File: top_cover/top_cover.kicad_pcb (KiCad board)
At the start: 2 copper layers, 323.6 x 142.9 mm, 82 parts, among them SW1 SW_Push, SW11 SW_Push, SW12 SW_Push, SW13 SW_Push, SW14 SW_Push, SW15 SW_Push, SW16 SW_Push, SW17 SW_Push, SW18 SW_Push, SW19 SW_Push, SW2 SW_Push, SW20 SW_Push, SW21 SW_Push, SW22 SW_Push, SW23 SW_Push, SW24 SW_Push, SW25 SW_Push, SW26 SW_Push, SW27 SW_Push, SW28 SW_Push, SW29 SW_Push, SW3 SW_Push, SW30 SW_Push, SW31 SW_Push, SW32 SW_Push, SW33 SW_Push, SW34 SW_Push, SW35 SW_Push, SW36 SW_Push, SW37 SW_Push, SW38 SW_Push, SW39 SW_Push, SW4 SW_Push, SW40 SW_Push, SW41 SW_Push, SW42 SW_Push, SW43 SW_Push, SW44 SW_Push, SW45 SW_Push, SW46 SW_Push, SW47 SW_Push, SW48 SW_Push, SW49 SW_Push, SW5 SW_Push, SW50 SW_Push, SW51 SW_Push, SW52 SW_Push, SW53 SW_Push, SW54 SW_Push, SW55 SW_Push, SW56 SW_Push, SW57 SW_Push, SW58 SW_Push, SW59 SW_Push, SW6 SW_Push, SW60 SW_Push, SW61 SW_Push, SW7 SW_Push, SW8 SW_Push, SW9 SW_Push

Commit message: Plates and covers
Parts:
- removed H1, H10, H11, H13, H15, H18, H19, H2, H21, H22, H4, H5, H6, H7: MountingHole, MountingHole:MountingHole_2.2mm_M2
- removed the H17 at (-40.4, 64.3)
- added H12: MountingHole, MountingHole:MountingHole_2.2mm_M2, B.Cu at (146.7, -58.3)
- added H16: MountingHole, MountingHole:MountingHole_2.2mm_M2, B.Cu at (159.4, -9.90)
- added H17: MountingHole, MountingHole:MountingHole_2.2mm_M2, B.Cu at (78.3, 57.5)
- added H17: MountingHole, MountingHole:MountingHole_2.2mm_M2, F.Cu at (-78.3, 57.5)
- added H20: MountingHole, MountingHole:MountingHole_2.2mm_M2, B.Cu at (47.0, -43.6)
- added H3: MountingHole, MountingHole:MountingHole_2.2mm_M2, B.Cu at (129.1, 34.1)
- added H8: MountingHole, MountingHole:MountingHole_2.2mm_M2, B.Cu at (99.7, -54.8)
- added H9: MountingHole, MountingHole:MountingHole_2.2mm_M2, B.Cu at (16.1, 79.6)
- moved H9 96.2 mm to (-16.1, 79.6)
- moved H12 37.6 mm to (-146.7, -58.3)
- moved H16 37.0 mm to (-159.4, -9.90)
- moved H8 26.6 mm to (-99.7, -54.8)
- moved H3 16.1 mm to (-129.1, 34.1)
- moved H20 9.74 mm to (-47.0, -43.6)
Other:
- outline, holes or cut-outs redrawn

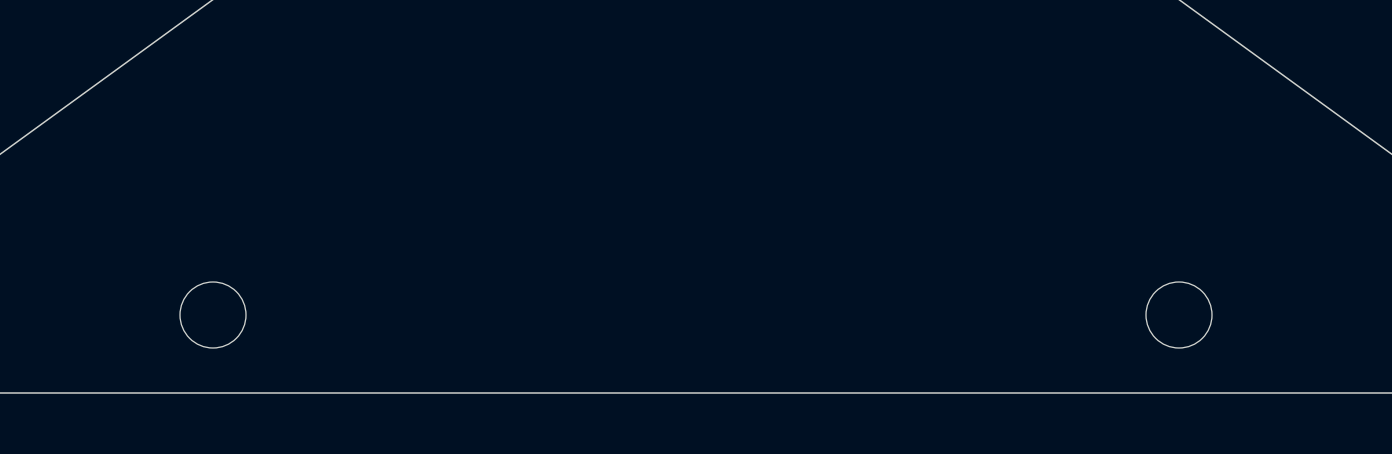
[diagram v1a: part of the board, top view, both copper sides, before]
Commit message: Moving mounting holes
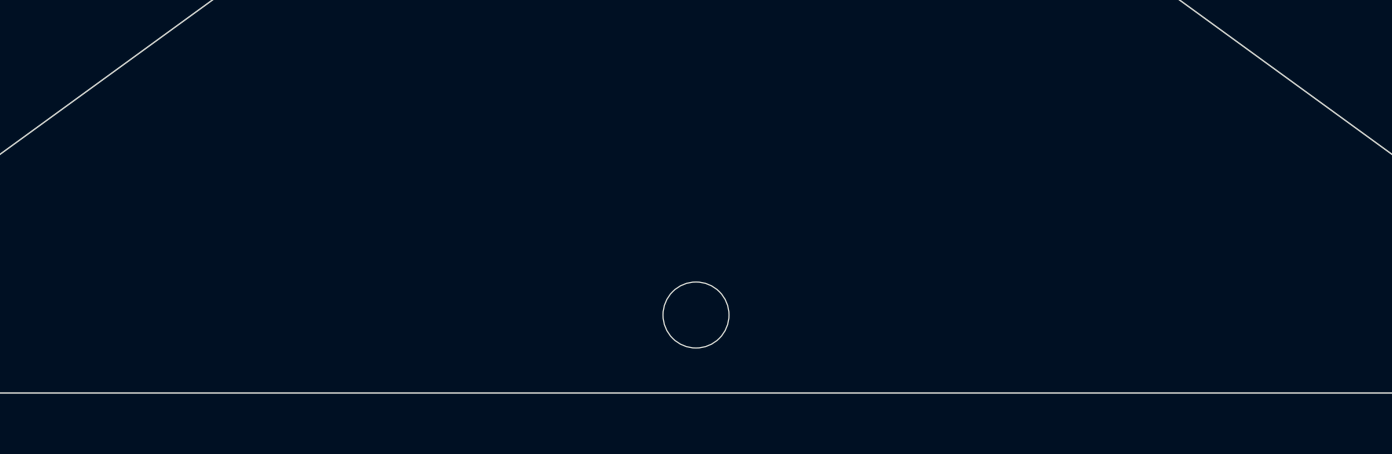
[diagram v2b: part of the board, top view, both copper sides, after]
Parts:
- removed the H9 at (-16.1, 79.6)
- moved H9 16.1 mm to (0.00, 79.6)

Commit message: Working on mounting holes
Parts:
- removed the H17 at (78.3, 57.5)
- added H17: MountingHole, MountingHole:MountingHole_2.2mm_M2, F.Cu at (101.6, 46.5)
- added H17: MountingHole, MountingHole:MountingHole_2.2mm_M2, F.Cu at (56.6, 67.2)
- added H17: MountingHole, MountingHole:MountingHole_2.2mm_M2, F.Cu at (-101.6, 46.5)
- H12, H16, H20, H3, H8, H9: moved to F.Cu
- moved H20 39.6 mm to (11.5, -26.1)
- moved H20 39.6 mm to (-11.5, -26.1)
- moved H8 26.7 mm to (73.2, -51.9)
- moved H8 26.7 mm to (-73.2, -51.9)
- moved H17 23.8 mm to (-56.6, 67.2)
- moved H3 16.6 mm to (-144.1, 27.1)
- moved H3 16.6 mm to (144.1, 27.1)
- moved H16 8.00 mm to (159.2, -17.9)
- moved H16 8.00 mm to (-159.2, -17.9)
- moved H12 0.63 mm to (146.1, -58.1)
- moved H12 0.63 mm to (-146.1, -58.1)

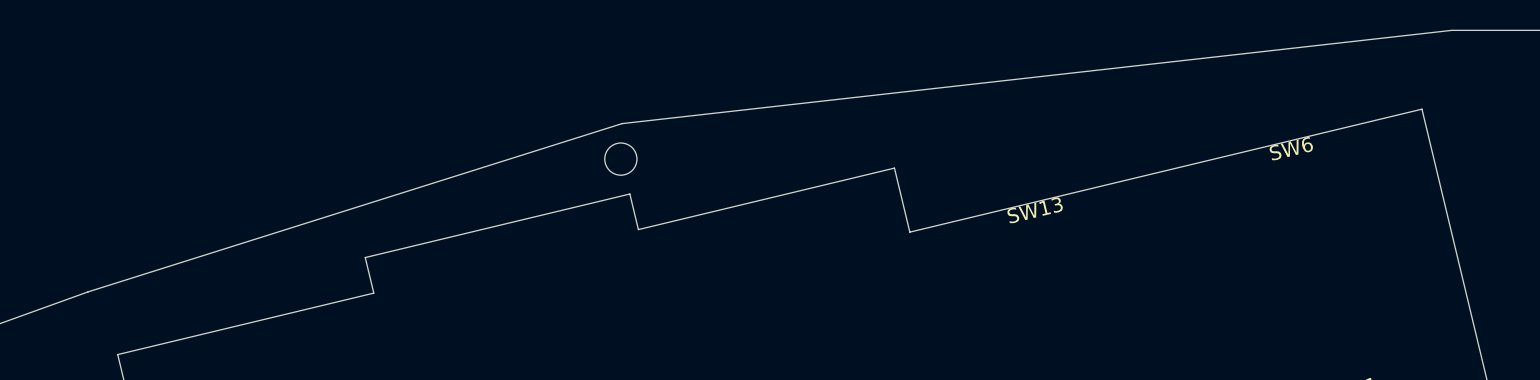
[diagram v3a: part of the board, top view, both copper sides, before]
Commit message: Mountin holes
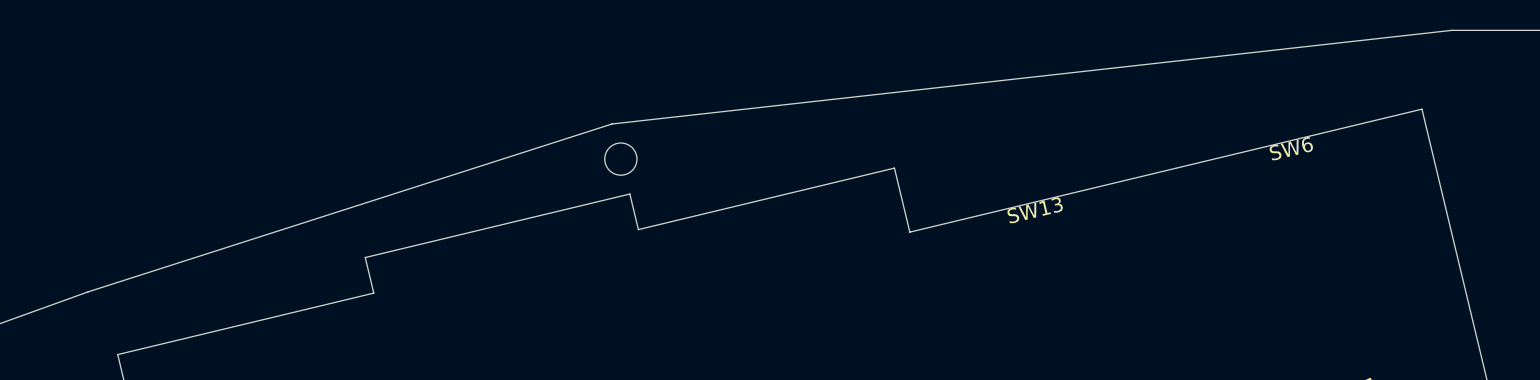
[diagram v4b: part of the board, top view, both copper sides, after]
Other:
- outline, holes or cut-outs redrawn

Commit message: Done with mounting holes, I guess.
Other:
- outline, holes or cut-outs redrawn

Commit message: Making the hole for the encoder optional
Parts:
- ENC2: footprint footprints:Switch_Hole -> footprints:Switch_Optional_Hole
- moved H16 110.9 mm to (109.4, -117.0), turned to 220.5 degrees
- moved H16 110.9 mm to (-132.7, 89.8), turned to 40.5 degrees
- moved H12 108.8 mm to (-148.8, 50.7), turned to 40.5 degrees
- moved H12 108.8 mm to (73.4, -139.1), turned to 220.5 degrees
- moved H3 101.5 mm to (-92.0, 114.2), turned to 40.5 degrees
- moved H3 101.5 mm to (127.2, -73.0), turned to 220.5 degrees
- moved SW53 92.0 mm to (104.3, -82.5), turned to 54 degrees
- moved SW46 92.0 mm to (-97.8, 90.1), turned to 27 degrees
- moved SW37 89.6 mm to (90.6, -92.4), turned to 54 degrees
- moved SW30 89.6 mm to (-105.5, 75.0), turned to 27 degrees
- moved SW6 89.2 mm to (63.0, -112.4), turned to 54 degrees
- moved SW1 89.2 mm to (-120.9, 44.7), turned to 27 degrees
- moved SW21 88.6 mm to (76.8, -102.4), turned to 54 degrees
- moved SW14 88.6 mm to (-113.2, 59.8), turned to 27 degrees
- moved SW61 80.1 mm to (93.7, -67.9), turned to 54 degrees
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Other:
- board size 323.6 x 142.9 mm -> 294.4 x 268.4 mm

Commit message: Working on top cover
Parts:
- removed ENC2: Switch Hole, footprints:Switch_Optional_Hole
- removed the H12 at (73.4, -139.1)
- removed the H12 at (-148.8, 50.7)
- removed the H16 at (109.4, -117.0)
- removed the H16 at (-132.7, 89.8)
- removed H17 (x4), H8 (x2), H9: MountingHole, MountingHole:MountingHole_2.2mm_M2
- removed the H20 at (-8.21, -27.3)
- removed the H20 at (-25.7, -12.4)
- removed the H3 at (127.2, -73.0)
- removed the H3 at (-92.0, 114.2)
- added ENC1: EVQWGD001, footprints:EVQWGD001, F.Cu at (-20.8, 21.9)
- added H1: MountingHole, MountingHole:MountingHole_2.2mm_M2, F.Cu at (-52.2, 70.5)
- added H10: MountingHole, MountingHole:MountingHole_2.2mm_M2, F.Cu at (0.00, 79.7)
- added H11: MountingHole, MountingHole:MountingHole_2.2mm_M2, F.Cu at (142.7, 26.1)
- added H12: MountingHole, MountingHole:MountingHole_2.2mm_M2, F.Cu at (-142.7, -64.2)
- added H13: MountingHole, MountingHole:MountingHole_2.2mm_M2, F.Cu at (-96.4, 48.8)
- added H15: MountingHole, MountingHole:MountingHole_2.2mm_M2, F.Cu at (168.2, -26.2)
- added H16: MountingHole, MountingHole:MountingHole_2.2mm_M2, F.Cu at (-168.2, -26.2)
- added H18: MountingHole, MountingHole:MountingHole_2.2mm_M2, F.Cu at (78.8, -57.8)
- added H2: MountingHole, MountingHole:MountingHole_2.2mm_M2, F.Cu at (52.2, 70.5)
- added H20: MountingHole, MountingHole:MountingHole_2.2mm_M2, F.Cu at (-78.8, -57.8)
- added H21: MountingHole, MountingHole:MountingHole_2.2mm_M2, F.Cu at (15.4, -37.8)
- added H22: MountingHole, MountingHole:MountingHole_2.2mm_M2, F.Cu at (142.7, -64.2)
- added H3: MountingHole, MountingHole:MountingHole_2.2mm_M2, F.Cu at (-142.7, 26.1)
- added H4: MountingHole, MountingHole:MountingHole_2.2mm_M2, F.Cu at (96.4, 48.8)
- added H6: MountingHole, MountingHole:MountingHole_2.2mm_M2, F.Cu at (-15.4, -37.8)
- moved SW46 98.9 mm to (-142.7, 2.04), turned to 349.5 degrees
- moved SW30 96.8 mm to (-139.4, -15.7), turned to 349.5 degrees
- moved SW1 96.5 mm to (-132.9, -51.1), turned to 349.5 degrees
- moved SW14 96.0 mm to (-136.2, -33.4), turned to 349.5 degrees
- moved SW6 93.0 mm to (132.9, -51.1), turned to 10.5 degrees
- moved SW53 92.8 mm to (142.7, 2.04), turned to 10.5 degrees
- moved SW21 91.1 mm to (136.2, -33.4), turned to 10.5 degrees
- moved SW37 91.0 mm to (139.4, -15.7), turned to 10.5 degrees
- moved SW54 87.4 mm to (-124.0, 5.51), turned to 349.5 degrees
- moved SW38 85.0 mm to (-120.8, -12.2), turned to 349.5 degrees
- moved SW7 84.6 mm to (-114.2, -47.6), turned to 349.5 degrees
- moved SW22 84.0 mm to (-117.5, -29.9), turned to 349.5 degrees
- moved SW13 79.6 mm to (114.2, -47.6), turned to 10.5 degrees
- moved SW61 79.4 mm to (124.0, 5.51), turned to 10.5 degrees
- moved SW29 77.4 mm to (117.5, -29.9), turned to 10.5 degrees
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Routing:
- net (no net): track 0.00 -> 1.48 mm
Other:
- board size 294.4 x 268.4 mm -> 341.3 x 148.9 mm
- board text added: "+"
- board text added: "-"

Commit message: Top plate is done
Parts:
- added ENC2: Switch Hole, footprints:Switch_Optional_Hole, F.Cu at (20.8, 21.9)
- ENC1: value EVQWGD001 -> Switch Hole; footprint footprints:EVQWGD001 -> footprints:Switch_Optional_Hole
- turned ENC1 to 319.5 degrees
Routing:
- net (no net): track 1.48 -> 0.00 mm
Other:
- outline, holes or cut-outs redrawn
- board text removed: "+"
- board text removed: "-"
